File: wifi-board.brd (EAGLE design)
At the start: 50 x 46 mm, 27 parts

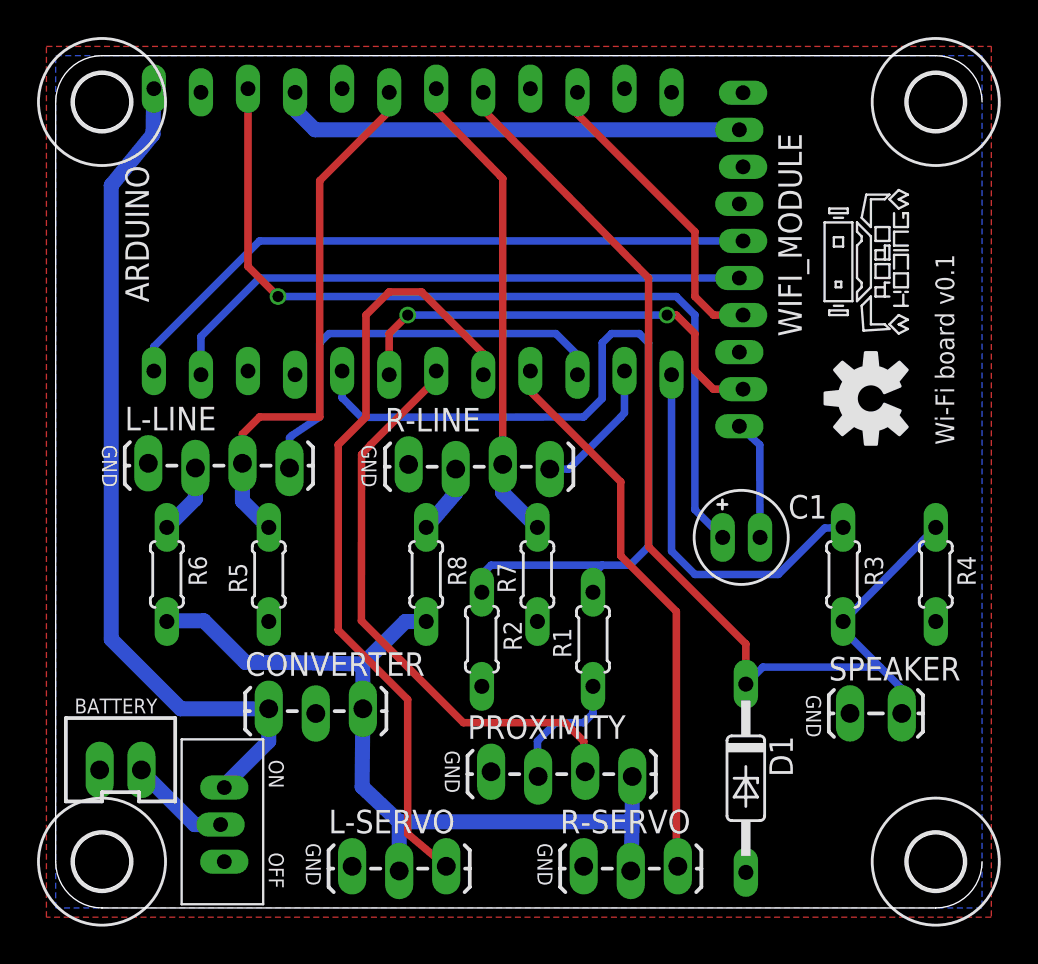
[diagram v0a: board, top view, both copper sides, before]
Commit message: updated power connector and resistors
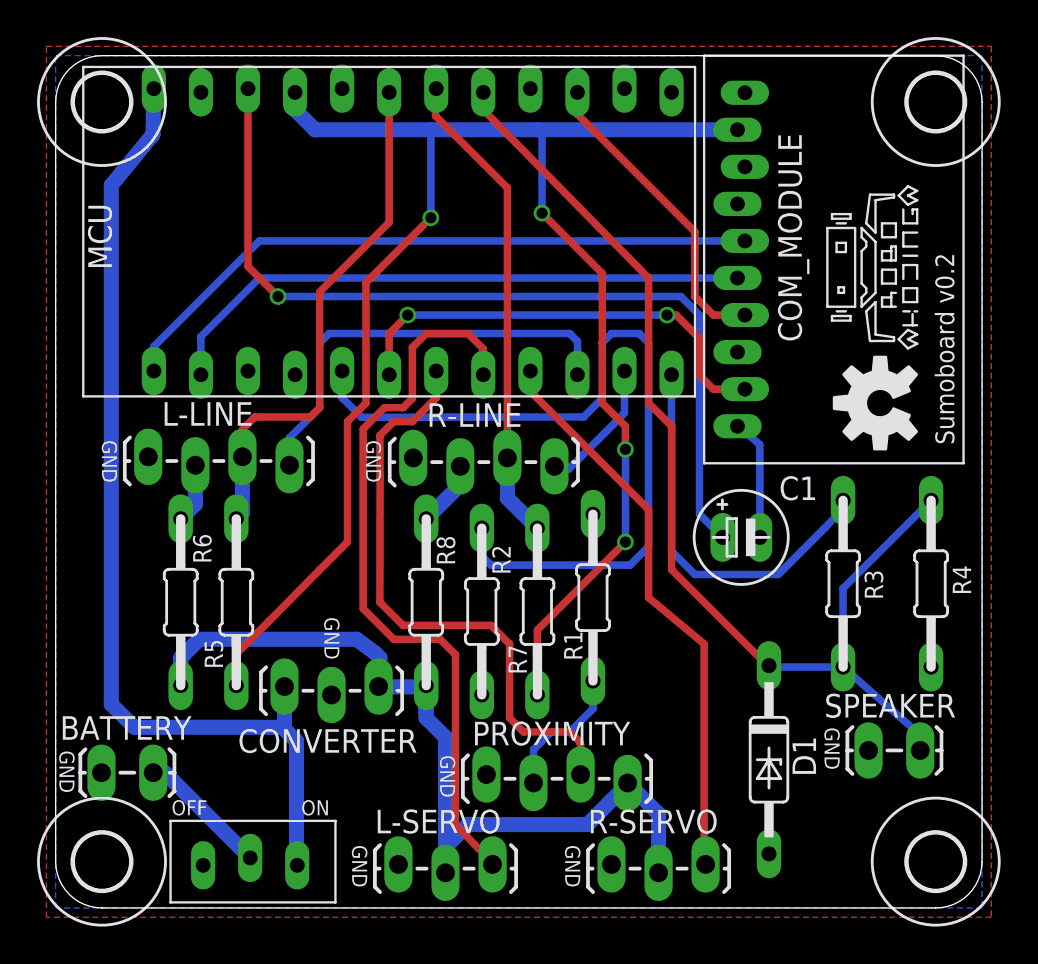
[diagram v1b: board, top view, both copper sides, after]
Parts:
- BATTERY: device SparkFun-Connectors:JST-2-PTH-VERT -> SparkFun-Connectors:1X02_LOCK_LONGPADS
- LOGO2: device Sumorobot:ROBOKODING-LOGO-M -> robokoding-logo:ROBOKODING-LOGO-M
- R5, R7: value 10K -> 4K7
- moved LOGO2 3.91 mm to (44.2, 34.5)
- moved L-SERVO 2.50 mm to (18.5, 2.25)
- moved POWER 2.50 mm to (10.5, 2.50), turned to 0 degrees
- moved R5 2.30 mm to (9.75, 16.5)
- moved R1 2.25 mm to (29.0, 16.8)
- moved SPEAKER 2.24 mm to (44.0, 8.50)
- moved R7 2.00 mm to (26.0, 16.0)
- moved R6 1.68 mm to (6.75, 16.5)
- moved D1 1.60 mm to (38.5, 8.00)
- moved R-SERVO 1.50 mm to (30.0, 2.25)
- moved R2 1.50 mm to (23.0, 16.0)
- moved R8 1.50 mm to (20.0, 16.5)
- moved CONVERTER 1.39 mm to (12.3, 11.8)
- moved BATTERY 1.14 mm to (2.60, 7.30)
- moved LOGO1 0.56 mm to (44.5, 27.2)
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- renumbered ARDUINO to MCU, WIFI_MODULE to COM_MODULE
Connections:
- net +3V3: now also R5.1, R7.1
- net GND: no longer R5.1, R7.1
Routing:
- net +3V3: track 25.3 -> 94.1 mm, vias 0 -> 4
- net VIN: track 45.9 -> 53.9 mm
- net D5: track 42.3 -> 39.8 mm
- net +5V: track 45.6 -> 47.7 mm
- net D2: track 45.5 -> 47.1 mm
- net BAT_IN: track 5.72 -> 7.14 mm
- net A2: track 29.3 -> 28.2 mm
- net D9: track 20.3 -> 21.2 mm
- net D4: track 31.5 -> 32.3 mm
- net D6: track 30.1 -> 30.8 mm
- net N$6: track 3.84 -> 3.22 mm
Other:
- board text added: "Sumoboard v0.2"
- board text removed: "Wi-Fi board v0.1"
